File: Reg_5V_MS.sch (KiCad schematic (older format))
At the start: 0 parts

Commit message: cleanup
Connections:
- net labels added: EN, VIN, VOUT
- net labels removed: VIN_3V3, VOUT_3V3
- wire segments 2 -> 3
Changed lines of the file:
@@
 LIBS:valves
 LIBS:hedgehog_symbols
+LIBS:switches
 LIBS:Hedgehog-cache
-EELAYER 25 0
+EELAYER 26 0
 EELAYER END
 $Descr A4 11693 8268
 encoding utf-8
-Sheet 8 8
+Sheet 2 8
 Title ""
 Date ""
@@
 Comment4 ""
 $EndDescr
-Text HLabel 1450 3050 0    60   Input ~ 0
-VIN_3V3
-Text HLabel 7100 3150 2    60   Output ~ 0
-VOUT_3V3
+Text HLabel 2250 2550 0    60   Input ~ 0
+VIN
+Text HLabel 6300 2600 2    60   Output ~ 0
+VOUT
 Wire Wire Line
-	1450 3050 2900 3050
+	2250 2550 3200 2550
 Wire Wire Line
-	7100 3150 6050 3150
+	6300 2600 5800 2600
+Text HLabel 2250 2050 0    60   Input ~ 0
+EN
+Wire Wire Line
+	2250 2050 3200 2050
 $EndSCHEMATC

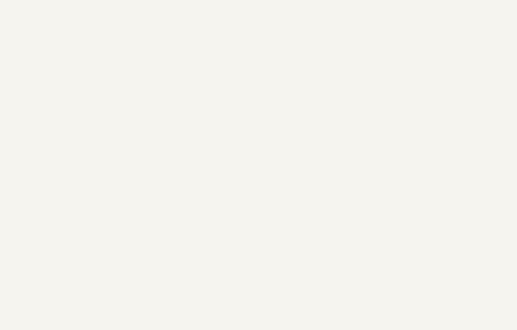
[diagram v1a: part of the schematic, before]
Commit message: added RPi Regulator added ref.des.-prefixes to all schematic sheets
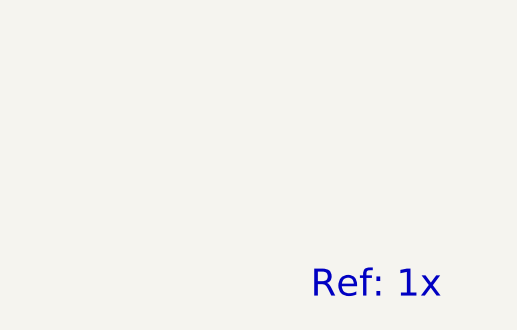
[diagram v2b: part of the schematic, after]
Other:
- note added: "Ref: 1x"
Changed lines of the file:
@@
 Wire Wire Line
 	2250 2050 3200 2050
+Text Notes 10550 6500 0    118  ~ 0
+Ref: 1x
 $EndSCHEMATC

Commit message: added note
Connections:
- net labels added: GND
- wire segments 3 -> 0
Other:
- note added: "TPS53319?"
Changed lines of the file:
@@
 Text HLabel 6300 2600 2    60   Output ~ 0
 VOUT
-Wire Wire Line
-	2250 2550 3200 2550
-Wire Wire Line
-	6300 2600 5800 2600
-Text HLabel 2250 2050 0    60   Input ~ 0
+Text HLabel 2200 2975 0    60   Input ~ 0
 EN
-Wire Wire Line
-	2250 2050 3200 2050
 Text Notes 10550 6500 0    118  ~ 0
 Ref: 1x
+$Comp
+L GND #PWR?
+U 1 1 5907589C
+P 4175 3725
+F 0 "#PWR?" H 4175 3475 50  0001 C CNN
+F 1 "GND" H 4180 3552 50  0000 C CNN
+F 2 "" H 4175 3725 50  0001 C CNN
+F 3 "" H 4175 3725 50  0001 C CNN
+	1    4175 3725
+	1    0    0    -1
+$EndComp
+Text Notes 3775 2900 0    60   ~ 0
+TPS53319?
 $EndSCHEMATC

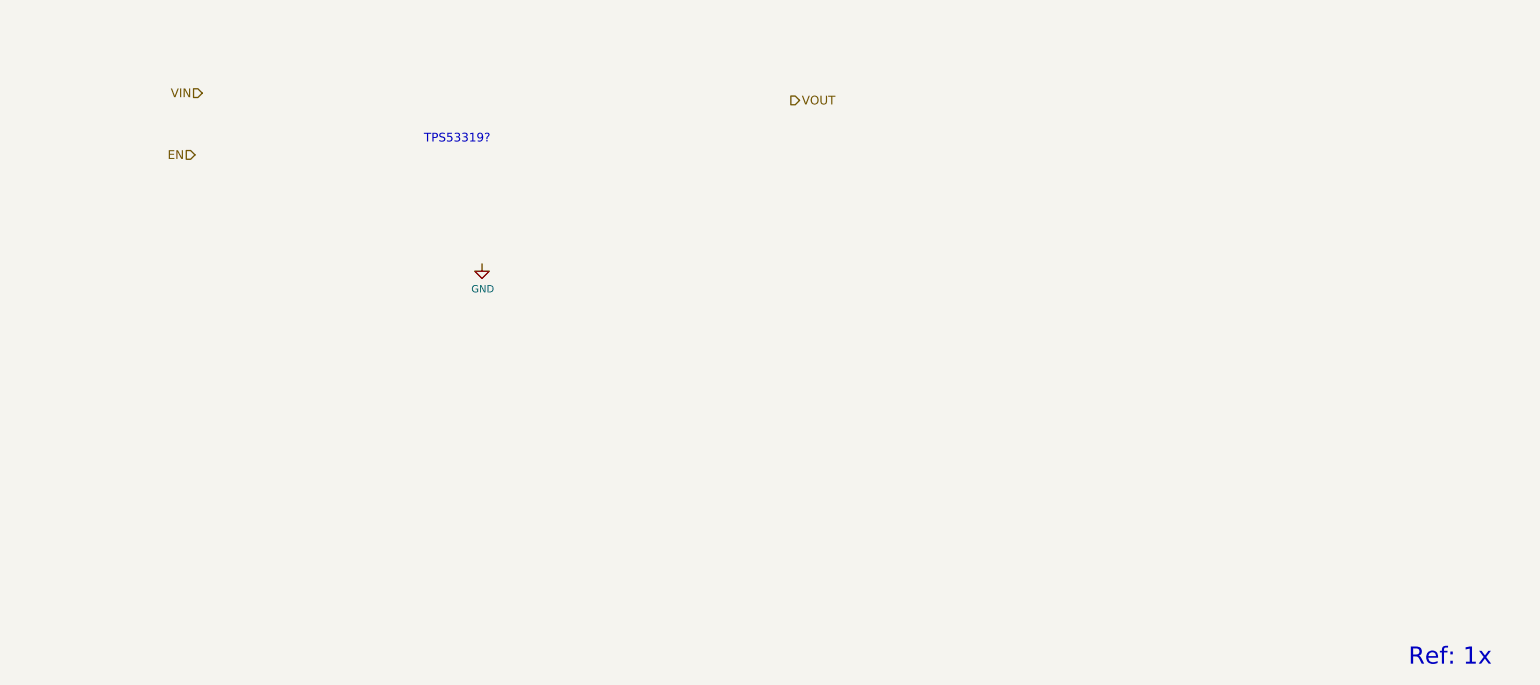
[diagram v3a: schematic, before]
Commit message: added Motor/Servo 5V regulator
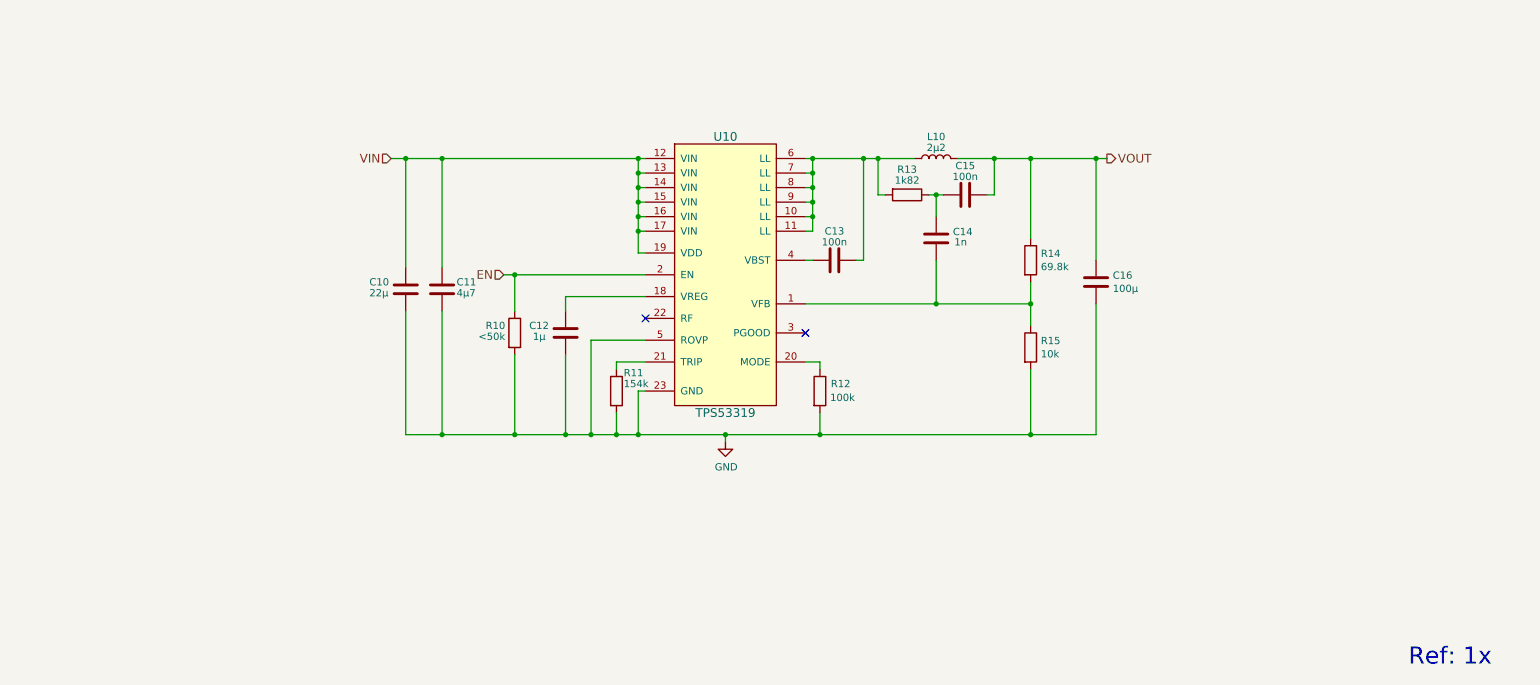
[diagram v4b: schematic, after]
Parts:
- added C10: 22µ, symbol C
- added C11: 4µ7, symbol C
- added C12: 1µ, symbol C
- added C13, C15: 100n, symbol C
- added C14: 1n, symbol C
- added C16: 100µ, symbol C
- added L10: 2µ2, symbol L
- added R10: <50k, symbol R
- added R11: 154k, symbol R
- added R12: 100k, symbol R
- added R13: 1k82, symbol R
- added R14: 69.8k, symbol R
- added R15: 10k, symbol R
- added U10: TPS53319, symbol TPS53319
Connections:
- net EN: now also R10.1, U10.2 (EN)
- net GND: now also C10.1, C11.1, C12.1, C16.1, R10.2, R11.2, R12.2, R15.2, U10.23 (GND), U10.5 (ROVP)
- net VIN: now also C10.2, C11.2, U10.12 (VIN), U10.13 (VIN), U10.14 (VIN), U10.15 (VIN), U10.16 (VIN), U10.17 (VIN), U10.19 (VDD)
- net VOUT: now also C15.2, C16.2, L10.2, R14.1
- new net: C14.2, R14.2, R15.1, U10.1 (VFB)
- new net: C13.2, L10.1, R13.2, U10.10 (LL), U10.11 (LL), U10.6 (LL), U10.7 (LL), U10.8 (LL), U10.9 (LL)
- new net: C12.2, U10.18 (VREG)
- new net: R12.1, U10.20 (MODE)
- new net: R11.1, U10.21 (TRIP)
- new net: C13.1, U10.4 (VBST)
- new net: C14.1, C15.1, R13.1
- no-connect marks 0 -> 2
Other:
- note removed: "TPS53319?"

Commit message: added HSOP-8,LSON-22,Mini-F3-B,MSOP-10,SOD323F Footprint finished package assignment (without inductors )
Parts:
- C10: footprint (none) -> Capacitors_SMD:C_1210_HandSoldering
- C11, C12: footprint (none) -> Capacitors_SMD:C_0603_HandSoldering
- C13, C14, C15: footprint (none) -> Capacitors_SMD:C_0805_HandSoldering
- C16: footprint (none) -> Capacitors_SMD:C_1206_HandSoldering
- R10, R11, R12, R13, R14, R15: footprint (none) -> Resistors_SMD:R_0402
- U10: footprint (none) -> hedgehog_footprints:LSON-22
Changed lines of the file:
@@
 F 0 "U10" H 5850 4750 60  0000 C CNN
 F 1 "TPS53319" H 5850 2850 60  0000 C CNN
-F 2 "" H 5850 3850 60  0001 C CNN
+F 2 "hedgehog_footprints:LSON-22" H 5850 3850 60  0001 C CNN
 F 3 "" H 5850 3850 60  0001 C CNN
 	1    5850 3800
@@
 F 0 "C10" H 3900 3850 50  0000 R CNN
 F 1 "22µ" H 3900 3925 50  0000 R CNN
-F 2 "" H 3688 3750 50  0001 C CNN
+F 2 "Capacitors_SMD:C_1210_HandSoldering" H 3688 3750 50  0001 C CNN
 F 3 "" H 3650 3900 50  0001 C CNN
 	1    3650 3900
@@
 F 0 "C11" H 3800 3850 50  0000 R CNN
 F 1 "4µ7" H 3800 3925 50  0000 R CNN
-F 2 "" H 3938 3750 50  0001 C CNN
+F 2 "Capacitors_SMD:C_0603_HandSoldering" H 3938 3750 50  0001 C CNN
 F 3 "" H 3900 3900 50  0001 C CNN
 	1    3900 3900
@@
 F 0 "C13" V 6800 3700 50  0000 C CNN
 F 1 "100n" V 6725 3700 50  0000 C CNN
-F 2 "" H 6638 3550 50  0001 C CNN
+F 2 "Capacitors_SMD:C_0805_HandSoldering" H 6638 3550 50  0001 C CNN
 F 3 "" H 6600 3700 50  0001 C CNN
 	1    6600 3700
@@
 F 0 "C14" H 7415 3596 50  0000 L CNN
 F 1 "1n" H 7425 3525 50  0000 L CNN
-F 2 "" H 7338 3400 50  0001 C CNN
+F 2 "Capacitors_SMD:C_0805_HandSoldering" H 7338 3400 50  0001 C CNN
 F 3 "" H 7300 3550 50  0001 C CNN
 	1    7300 3550
@@
 F 0 "C15" V 7700 3250 50  0000 C CNN
 F 1 "100n" V 7625 3250 50  0000 C CNN
-F 2 "" H 7538 3100 50  0001 C CNN
+F 2 "Capacitors_SMD:C_0805_HandSoldering" H 7538 3100 50  0001 C CNN
 F 3 "" H 7500 3250 50  0001 C CNN
 	1    7500 3250
@@
 F 0 "C16" H 8285 3804 50  0000 R CNN
 F 1 "100µ" H 8285 3895 50  0000 R CNN
-F 2 "" H 8438 3700 50  0001 C CNN
+F 2 "Capacitors_SMD:C_1206_HandSoldering" H 8438 3700 50  0001 C CNN
 F 3 "" H 8400 3850 50  0001 C CNN
 	1    8400 3850
@@
 F 0 "R10" H 4200 4250 50  0000 L CNN
 F 1 "<50k" H 4150 4175 50  0000 L CNN
-F 2 "" V 4330 4200 50  0001 C CNN
+F 2 "Resistors_SMD:R_0402" V 4330 4200 50  0001 C CNN
 F 3 "" H 4400 4200 50  0001 C CNN
 	1    4400 4200
@@
 F 0 "C12" H 5000 4150 50  0000 R CNN
 F 1 "1µ" H 4975 4225 50  0000 R CNN
-F 2 "" H 4788 4050 50  0001 C CNN
+F 2 "Capacitors_SMD:C_0603_HandSoldering" H 4788 4050 50  0001 C CNN
 F 3 "" H 4750 4200 50  0001 C CNN
 	1    4750 4200
@@
 F 0 "R11" H 5150 4725 50  0000 L CNN
 F 1 "154k" H 5150 4650 50  0000 L CNN
-F 2 "" V 5030 4600 50  0001 C CNN
+F 2 "Resistors_SMD:R_0402" V 5030 4600 50  0001 C CNN
 F 3 "" H 5100 4600 50  0001 C CNN
 	1    5100 4600
@@
 F 0 "R12" H 6575 4650 50  0000 L CNN
 F 1 "100k" H 6570 4555 50  0000 L CNN
-F 2 "" V 6430 4600 50  0001 C CNN
+F 2 "Resistors_SMD:R_0402" V 6430 4600 50  0001 C CNN
 F 3 "" H 6500 4600 50  0001 C CNN
 	1    6500 4600
@@
 F 0 "R13" V 6925 3250 50  0000 C CNN
 F 1 "1k82" V 7000 3250 50  0000 C CNN
-F 2 "" V 7030 3250 50  0001 C CNN
+F 2 "Resistors_SMD:R_0402" V 7030 3250 50  0001 C CNN
 F 3 "" H 7100 3250 50  0001 C CNN
 	1    7100 3250
@@
 F 0 "R14" H 8020 3746 50  0000 L CNN
 F 1 "69.8k" H 8020 3655 50  0000 L CNN
-F 2 "" V 7880 3700 50  0001 C CNN
+F 2 "Resistors_SMD:R_0402" V 7880 3700 50  0001 C CNN
 F 3 "" H 7950 3700 50  0001 C CNN
 	1    7950 3700
@@
 F 0 "R15" H 8020 4346 50  0000 L CNN
 F 1 "10k" H 8020 4255 50  0000 L CNN
-F 2 "" V 7880 4300 50  0001 C CNN
+F 2 "Resistors_SMD:R_0402" V 7880 4300 50  0001 C CNN
 F 3 "" H 7950 4300 50  0001 C CNN
 	1    7950 4300
